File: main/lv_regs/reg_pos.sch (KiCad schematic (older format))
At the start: 10 parts, among them M1 ﻿APXW003A0X3-SRZ

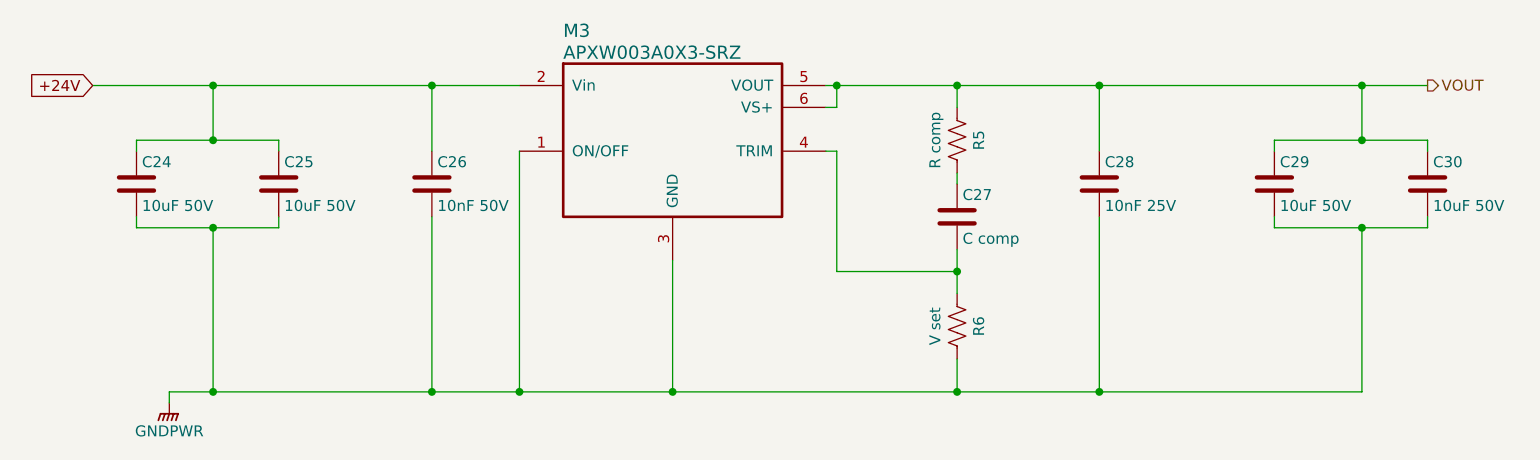
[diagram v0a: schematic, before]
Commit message: A near final version of the low-volt regulator board. Pending footprint comparison on the actual parts.
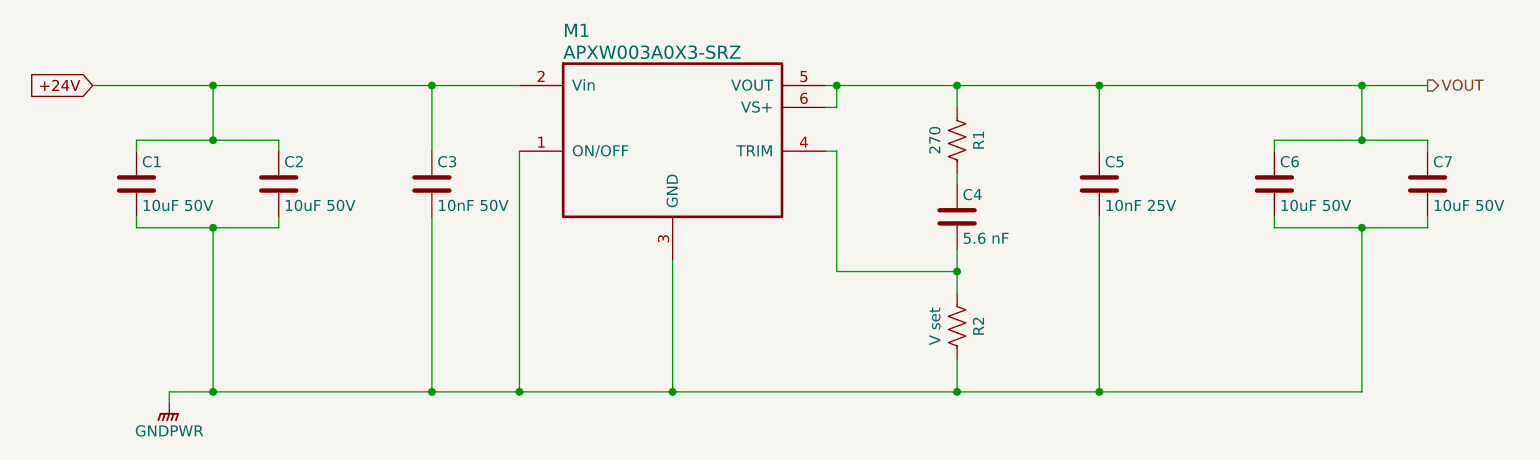
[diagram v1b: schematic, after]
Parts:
- C1, C2, C6, C7: DK line (none) -> P.4
- C3: DK line (none) -> P.5
- C4: value C comp -> 5.6 nF
- C5: DK line (none) -> P.2
- M1: DK line (none) -> P.1
- R1: value R comp -> 270
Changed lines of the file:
@@
 $Descr A4 11693 8268
 encoding utf-8
-Sheet 3 4
+Sheet 4 4
 Title ""
 Date ""
@@
 AR Path="/5F20EA50/5F20EFB5" Ref="M1"  Part="1"
 AR Path="/5F238A75/5F20EFB5" Ref="M3"  Part="1"
-F 0 "M3" H 5650 3050 60  0000 L CNN
+F 0 "M1" H 5650 3050 60  0000 L CNN
 F 1 "﻿APXW003A0X3-SRZ" H 5650 2950 60  0000 L CNN
 F 2 "lv_regs:APXW003A0X3-SRZ" H 5650 2850 60  0001 L CNN
@@
 F 6 "APXW003A0X3-SRZ" H 5450 2800 50  0001 C CNN "MPN"
 F 7 "ABB Power Electronics Inc." H 5450 2800 50  0001 C CNN "Manufacturer"
+F 8 "P.1" H 5450 2800 50  0001 C CNN "DK line"
 	1    5450 2800
 	1    0    0    -1
@@
 AR Path="/5F20EA50/5F20EFC1" Ref="C5"  Part="1"
 AR Path="/5F238A75/5F20EFC1" Ref="C28"  Part="1"
-F 0 "C28" H 8125 3350 50  0000 L CNN
+F 0 "C5" H 8125 3350 50  0000 L CNN
 F 1 "10nF 25V" H 8125 3150 50  0000 L CNN
 F 2 "lv_regs:cap_smd_0306" H 8138 3100 50  0001 C CNN
@@
 F 6 "LLL185R71E103MA01L" H 8100 3250 50  0001 C CNN "MPN"
 F 7 "Murata Electronics" H 8100 3250 50  0001 C CNN "Manufacturer"
+F 8 "P.2" H 8100 3250 50  0001 C CNN "DK line"
 	1    8100 3250
 	1    0    0    -1
@@
 AR Path="/5F20EA50/5F20EFC7" Ref="C3"  Part="1"
 AR Path="/5F238A75/5F20EFC7" Ref="C26"  Part="1"
-F 0 "C26" H 5075 3350 50  0000 L CNN
+F 0 "C3" H 5075 3350 50  0000 L CNN
 F 1 "10nF 50V" H 5075 3150 50  0000 L CNN
 F 2 "Capacitor_SMD:C_0603_1608Metric" H 5088 3100 50  0001 C CNN
@@
 F 6 "C0603C103M5RACTU" H 5050 3250 50  0001 C CNN "MPN"
 F 7 "KEMET" H 5050 3250 50  0001 C CNN "Manufacturer"
+F 8 "P.5" H 5050 3250 50  0001 C CNN "DK line"
 	1    5050 3250
 	1    0    0    -1
@@
 AR Path="/5F20EA50/5F20EFCD" Ref="C1"  Part="1"
 AR Path="/5F238A75/5F20EFCD" Ref="C24"  Part="1"
-F 0 "C24" H 3725 3350 50  0000 L CNN
+F 0 "C1" H 3725 3350 50  0000 L CNN
 F 1 "10uF 50V" H 3725 3150 50  0000 L CNN
 F 2 "Capacitor_SMD:C_1210_3225Metric" H 3738 3100 50  0001 C CNN
@@
 F 6 "CL32B106KBJNNNE" H 3700 3250 50  0001 C CNN "MPN"
 F 7 "Samsung Electro-Mechanics" H 3700 3250 50  0001 C CNN "Manufacturer"
+F 8 "P.4" H 3700 3250 50  0001 C CNN "DK line"
 	1    3700 3250
 	1    0    0    -1
@@
 AR Path="/5F20EA50/5F20EFD3" Ref="C2"  Part="1"
 AR Path="/5F238A75/5F20EFD3" Ref="C25"  Part="1"
-F 0 "C25" H 4375 3350 50  0000 L CNN
+F 0 "C2" H 4375 3350 50  0000 L CNN
 F 1 "10uF 50V" H 4375 3150 50  0000 L CNN
 F 2 "Capacitor_SMD:C_1210_3225Metric" H 4388 3100 50  0001 C CNN
@@
 F 6 "CL32B106KBJNNNE" H 4350 3250 50  0001 C CNN "MPN"
 F 7 "Samsung Electro-Mechanics" H 4350 3250 50  0001 C CNN "Manufacturer"
+F 8 "P.4" H 4350 3250 50  0001 C CNN "DK line"
 	1    4350 3250
 	1    0    0    -1
@@
 AR Path="/5F20EA50/5F20EFE6" Ref="R1"  Part="1"
 AR Path="/5F238A75/5F20EFE6" Ref="R5"  Part="1"
-F 0 "R5" V 7550 3050 50  0000 C CNN
-F 1 "R comp" V 7350 3050 50  0000 C CNN
+F 0 "R1" V 7550 3050 50  0000 C CNN
+F 1 "270" V 7350 3050 50  0000 C CNN
 F 2 "Resistor_SMD:R_0603_1608Metric" V 7490 3040 50  0001 C CNN
 F 3 "~" H 7450 3050 50  0001 C CNN
@@
 AR Path="/5F20EA50/5F20EFEC" Ref="R2"  Part="1"
 AR Path="/5F238A75/5F20EFEC" Ref="R6"  Part="1"
-F 0 "R6" V 7550 3900 50  0000 C CNN
+F 0 "R2" V 7550 3900 50  0000 C CNN
 F 1 "V set" V 7350 3900 50  0000 C CNN
 F 2 "Resistor_SMD:R_0603_1608Metric" V 7490 3890 50  0001 C CNN
@@
 AR Path="/5F20EA50/5F20EFF2" Ref="C4"  Part="1"
 AR Path="/5F238A75/5F20EFF2" Ref="C27"  Part="1"
-F 0 "C27" H 7475 3500 50  0000 L CNN
-F 1 "C comp" H 7475 3300 50  0000 L CNN
+F 0 "C4" H 7475 3500 50  0000 L CNN
+F 1 "5.6 nF" H 7475 3300 50  0000 L CNN
 F 2 "Capacitor_SMD:C_0603_1608Metric" H 7488 3250 50  0001 C CNN
 F 3 "~" H 7450 3400 50  0001 C CNN
@@
 AR Path="/5F20EA50/5F20F022" Ref="C7"  Part="1"
 AR Path="/5F238A75/5F20F022" Ref="C30"  Part="1"
-F 0 "C30" H 9625 3350 50  0000 L CNN
+F 0 "C7" H 9625 3350 50  0000 L CNN
 F 1 "10uF 50V" H 9625 3150 50  0000 L CNN
 F 2 "Capacitor_SMD:C_1210_3225Metric" H 9638 3100 50  0001 C CNN
@@
 F 6 "CL32B106KBJNNNE" H 9600 3250 50  0001 C CNN "MPN"
 F 7 "Samsung Electro-Mechanics" H 9600 3250 50  0001 C CNN "Manufacturer"
+F 8 "P.4" H 9600 3250 50  0001 C CNN "DK line"
 	1    9600 3250
 	1    0    0    -1
@@
 AR Path="/5F20EA50/5F21128F" Ref="#PWR01"  Part="1"
 AR Path="/5F238A75/5F21128F" Ref="#PWR016"  Part="1"
-F 0 "#PWR016" H 3850 4050 50  0001 C CNN
+F 0 "#PWR01" H 3850 4050 50  0001 C CNN
 F 1 "GNDPWR" H 3850 4120 50  0000 C CNN
 F 2 "" H 3850 4200 50  0001 C CNN
@@
 AR Path="/5F20EA50/5F20F01C" Ref="C6"  Part="1"
 AR Path="/5F238A75/5F20F01C" Ref="C29"  Part="1"
-F 0 "C29" H 8925 3350 50  0000 L CNN
+F 0 "C6" H 8925 3350 50  0000 L CNN
 F 1 "10uF 50V" H 8925 3150 50  0000 L CNN
 F 2 "Capacitor_SMD:C_1210_3225Metric" H 8938 3100 50  0001 C CNN
@@
 F 6 "CL32B106KBJNNNE" H 8900 3250 50  0001 C CNN "MPN"
 F 7 "Samsung Electro-Mechanics" H 8900 3250 50  0001 C CNN "Manufacturer"
+F 8 "P.4" H 8900 3250 50  0001 C CNN "DK line"
 	1    8900 3250
 	1    0    0    -1

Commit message: Schematic revision for DAC board, compensation tweaks in lv_regs.
Opamp +/- pins were swapped in reference_buffer.sch as side effect of the symbol change from using a dual opamp.

lv_regs files.  The compensation components were (CTUNE/RTUNE) were quite wrong, and everything oscillated like crazy. The positive regulators are fine with no compensation, and the negative regulator benefits from a bit.
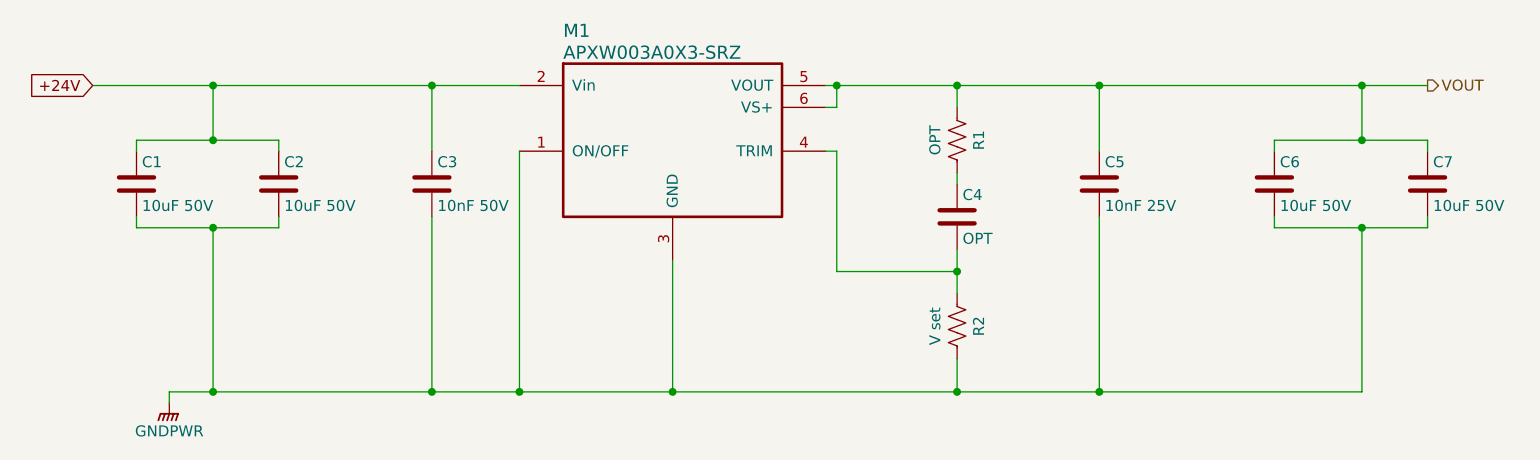
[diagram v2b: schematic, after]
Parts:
- C4: value 5.6 nF -> OPT
- R1: value 270 -> OPT
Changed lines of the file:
@@
 AR Path="/5F238A75/5F20EFE6" Ref="R5"  Part="1"
 F 0 "R1" V 7550 3050 50  0000 C CNN
-F 1 "270" V 7350 3050 50  0000 C CNN
+F 1 "OPT" V 7350 3050 50  0000 C CNN
 F 2 "Resistor_SMD:R_0603_1608Metric" V 7490 3040 50  0001 C CNN
 F 3 "~" H 7450 3050 50  0001 C CNN
@@
 AR Path="/5F238A75/5F20EFF2" Ref="C27"  Part="1"
 F 0 "C4" H 7475 3500 50  0000 L CNN
-F 1 "5.6 nF" H 7475 3300 50  0000 L CNN
+F 1 "OPT" H 7475 3300 50  0000 L CNN
 F 2 "Capacitor_SMD:C_0603_1608Metric" H 7488 3250 50  0001 C CNN
 F 3 "~" H 7450 3400 50  0001 C CNN
